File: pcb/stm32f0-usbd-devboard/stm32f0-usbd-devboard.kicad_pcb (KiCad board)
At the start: 2 copper layers, 23.1 x 51.9 mm, 24 parts, among them J1 USB_B_Mini, J2 PIN H 5P, J3 LEFT, J4 RIGHT, U1 USBLC6-2SC6, U2 MCP1700-3302E, U3 STM32F042K4T6 or STM32F042K6T6

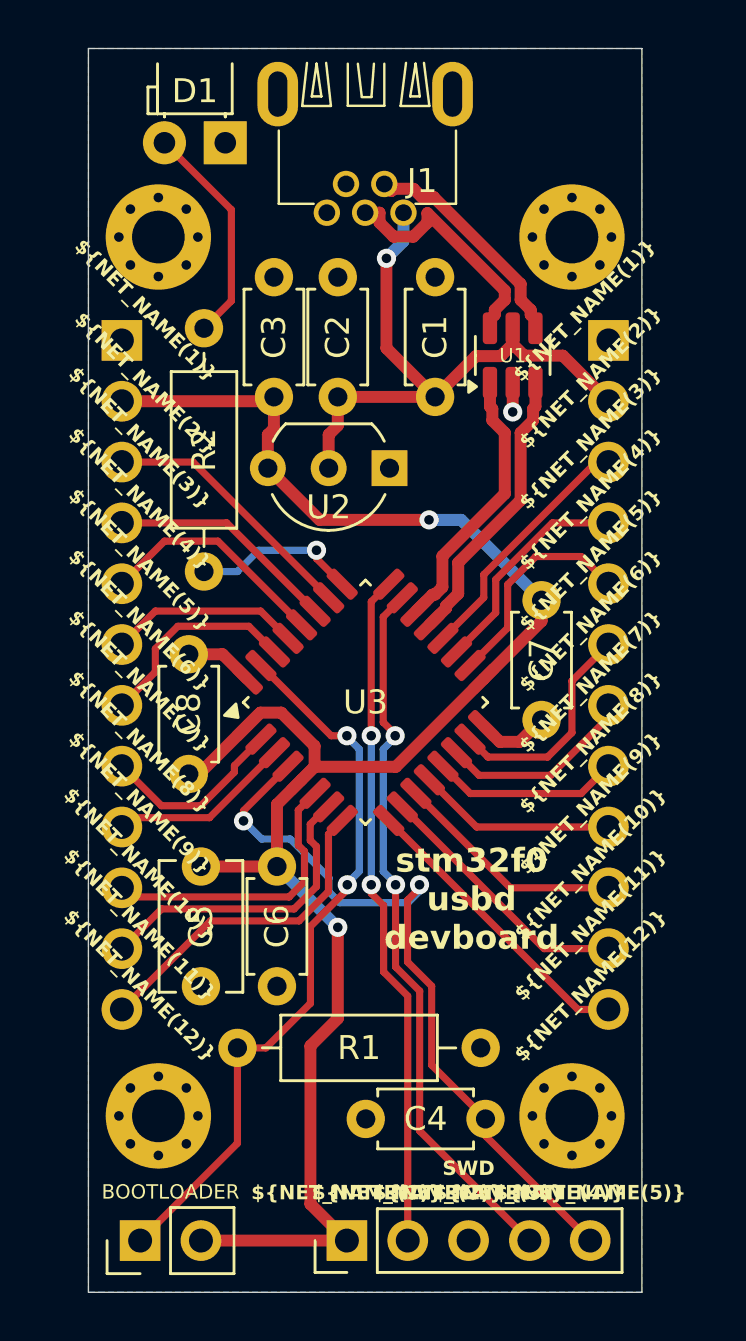
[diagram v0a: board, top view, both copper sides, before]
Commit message: pcb: *: new revision: 20250412
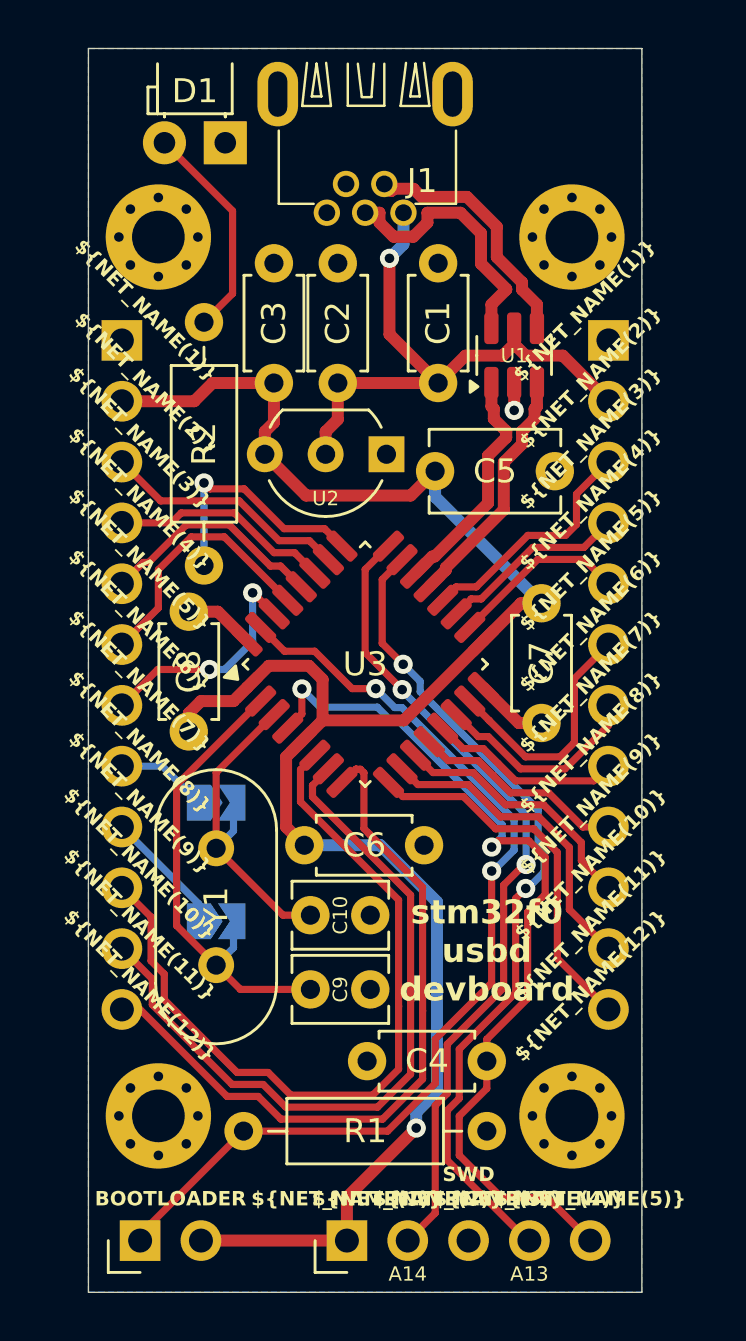
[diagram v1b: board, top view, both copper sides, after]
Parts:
- added C10: 12p, Capacitor_THT:C_Disc_D3.8mm_W2.6mm_P2.50mm, F.Cu at (144.8, 114.6)
- added C9: 12p, Capacitor_THT:C_Disc_D3.8mm_W2.6mm_P2.50mm, F.Cu at (144.8, 117.7)
- added J5: BOOTLOADER, custom:PinHeader_Bootloader_1x02_P2.54mm_Horizontal, F.Cu at (137.7, 128.1)
- added JP2: Connect Pin F0 to PF0, Jumper:SolderJumper-2_P1.3mm_Open_TrianglePad1.0x1.5mm, B.Cu at (140.8, 114.8)
- added Y1: 8MHz, Crystal:Crystal_HC49-4H_Vertical, F.Cu at (140.8, 111.8)
- H1, H2, H3, H4: value MountingHole_Pad -> Mounting Hole
- JP1: value BOOTLOADER -> Connect Pin F1 to PF1; footprint Connector_PinHeader_2.54mm:PinHeader_1x02_P2.54mm_Vertical -> Jumper:SolderJumper-2_P1.3mm_Open_TrianglePad1.0x1.5mm; moved to B.Cu
- moved C5 26.1 mm to (155.0, 96.0), turned to 180 degrees
- moved JP1 18.6 mm to (140.8, 109.9), turned to 0 degrees
- moved C6 8.51 mm to (149.5, 111.6), turned to 180 degrees
- moved R1 3.48 mm to (142.0, 123.6)
- moved C4 2.41 mm to (147.1, 120.7)
- moved REF** 2.36 mm to (147.1, 100.9)
- moved C8 1.78 mm to (139.7, 101.9)
- moved U3 1.59 mm to (147.1, 104.1)
- moved C1 0.59 mm to (150.1, 87.3)
- moved U2 0.59 mm to (148.0, 95.3)
- moved C2 0.58 mm to (145.9, 87.3)
- moved C3 0.58 mm to (143.3, 87.3)
- moved R2 0.25 mm to (140.3, 99.9)
- moved C7 0.13 mm to (154.4, 106.5)
- moved U1 0.06 mm to (153.3, 91.2)
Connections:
- J3 pad 8: F0 -> F1
- J3 pad 9: F1 -> F0
- JP1 pad 1: Net-(JP1-A) -> F1
- JP1 pad 2: 3.3V -> PF1
- R1 pad 1: Net-(JP1-A) -> Net-(J5-Pin_1)
- U3 pad 2: F0 -> PF0
- U3 pad 3: F1 -> PF1
- U3 pad 31: Net-(JP1-A) -> Net-(J5-Pin_1)
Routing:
- net Net-(J5-Pin_1): track 0.00 -> 41.5 mm, vias 0 -> 2
- net Net-(JP1-A): track 30.6 -> 0.00 mm, vias 2 -> 0
- net A0: track 12.1 -> 32.3 mm
- net PF0: track 0.00 -> 19.7 mm
- net A1: track 13.0 -> 30.7 mm
- net A2: track 13.9 -> 30.3 mm
- net PF1: track 0.00 -> 13.9 mm
- net NRST: track 30.9 -> 37.3 mm
- net CLK: track 28.3 -> 34.6 mm
- net DIO: track 30.1 -> 34.8 mm
- net 3.3V: track 75.7 -> 80.2 mm, vias 2 -> 1
- net LED: track 6.93 -> 10.4 mm
- net F1: track 7.66 -> 4.35 mm
- net A3: track 12.4 -> 15.7 mm
- net B6: track 7.99 -> 10.8 mm
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
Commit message: pcb: f0: fix crystal capacitor values
trivial fix not affecting any physical layers, not bumping revision.
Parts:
- C10, C9: value 12p -> 22p
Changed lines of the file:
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@@
 			)
 		)
-		(property "Value" "12p"
+		(property "Value" "22p"
 			(at 1.25 2.55 0)
 			(layer "F.Fab")
@@
 			)
 		)
-		(property "Value" "12p"
+		(property "Value" "22p"
 			(at 1.25 2.55 0)
 			(layer "F.Fab")

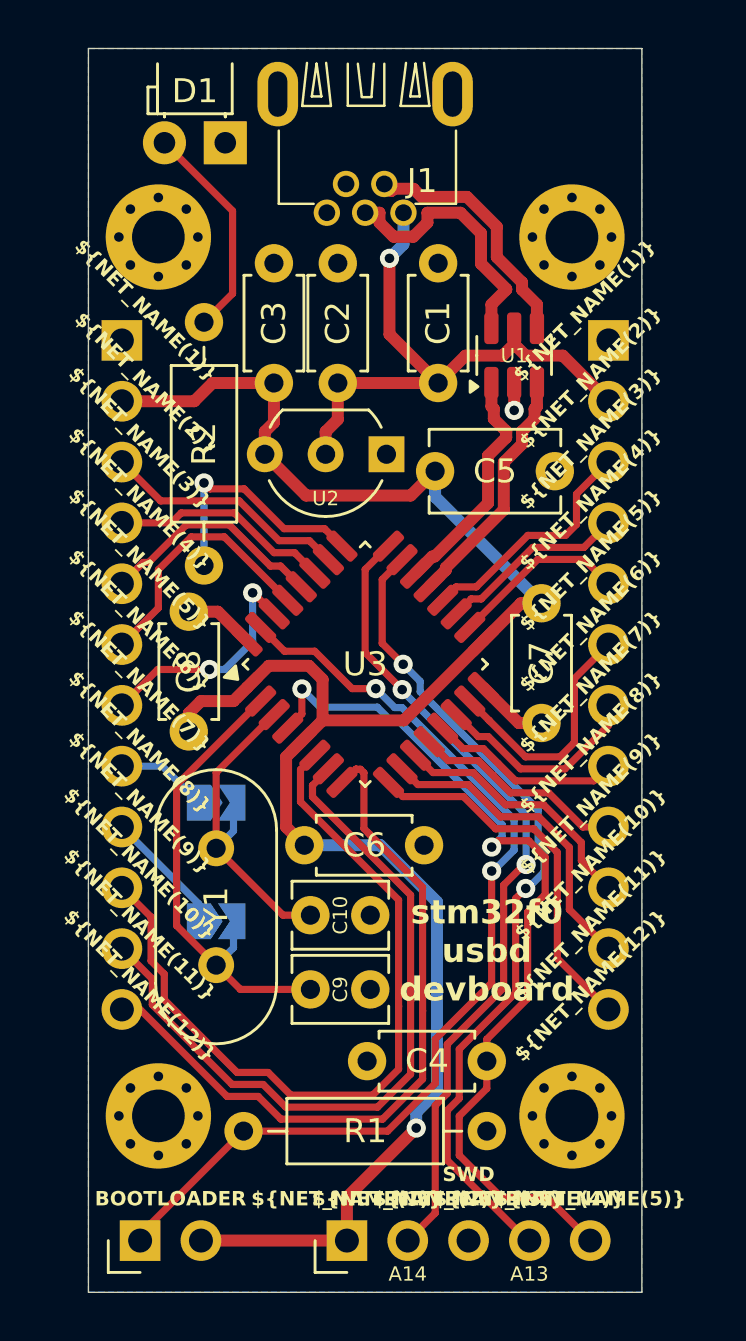
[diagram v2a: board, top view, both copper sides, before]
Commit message: pcb: f0: upgrade to kicad 10
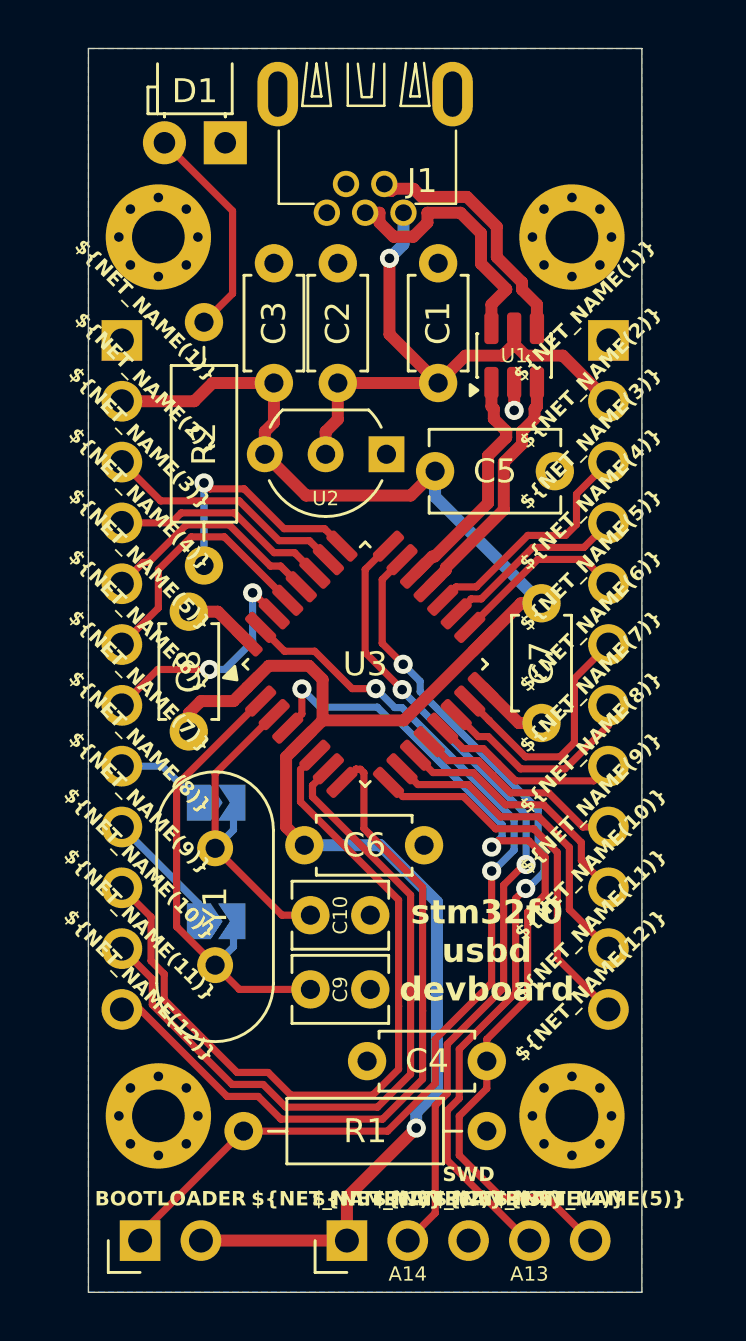
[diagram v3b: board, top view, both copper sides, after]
